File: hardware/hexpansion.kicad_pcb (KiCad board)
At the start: 2 copper layers, 86 x 45.6 mm, 87 parts, among them J1 Hexpansion-Connector, U1 AP3602AKTR-G1, U10 XL-0807RGBC-WS2812B-S, U11 XL-0807RGBC-WS2812B-S, U12 XL-0807RGBC-WS2812B-S, U13 XL-0807RGBC-WS2812B-S, U14 XL-0807RGBC-WS2812B-S, U15 XL-0807RGBC-WS2812B-S, U16 XL-0807RGBC-WS2812B-S, U17 XL-0807RGBC-WS2812B-S, U18 XL-0807RGBC-WS2812B-S, U19 XL-0807RGBC-WS2812B-S, U2 ZD24C64A-XGMT, U20 XL-0807RGBC-WS2812B-S, U21 XL-0807RGBC-WS2812B-S, U22 XL-0807RGBC-WS2812B-S, U23 XL-0807RGBC-WS2812B-S, U24 XL-0807RGBC-WS2812B-S, U25 XL-0807RGBC-WS2812B-S, U26 XL-0807RGBC-WS2812B-S, U27 XL-0807RGBC-WS2812B-S, U28 XL-0807RGBC-WS2812B-S, U29 XL-0807RGBC-WS2812B-S, U3 XL-0807RGBC-WS2812B-S, U30 XL-0807RGBC-WS2812B-S, U31 XL-0807RGBC-WS2812B-S, U32 XL-0807RGBC-WS2812B-S, U33 XL-0807RGBC-WS2812B-S, U34 XL-0807RGBC-WS2812B-S, U35 XL-0807RGBC-WS2812B-S, U36 XL-0807RGBC-WS2812B-S, U37 XL-0807RGBC-WS2812B-S, U38 XL-0807RGBC-WS2812B-S, U39 XL-0807RGBC-WS2812B-S, U4 XL-0807RGBC-WS2812B-S, U40 XL-0807RGBC-WS2812B-S, U41 XL-0807RGBC-WS2812B-S, U42 XL-0807RGBC-WS2812B-S, U43 XL-0807RGBC-WS2812B-S, U44 XL-0807RGBC-WS2812B-S, U45 XL-0807RGBC-WS2812B-S, U46 XL-0807RGBC-WS2812B-S, U47 XL-0807RGBC-WS2812B-S, U48 XL-0807RGBC-WS2812B-S, U49 XL-0807RGBC-WS2812B-S, U5 XL-0807RGBC-WS2812B-S, U50 XL-0807RGBC-WS2812B-S, U51 XL-0807RGBC-WS2812B-S, U52 XL-0807RGBC-WS2812B-S, U53 XL-0807RGBC-WS2812B-S, U54 XL-0807RGBC-WS2812B-S, U55 XL-0807RGBC-WS2812B-S, U56 XL-0807RGBC-WS2812B-S, U57 XL-0807RGBC-WS2812B-S, U58 XL-0807RGBC-WS2812B-S, U59 XL-0807RGBC-WS2812B-S, U6 XL-0807RGBC-WS2812B-S, U60 XL-0807RGBC-WS2812B-S, U61 XL-0807RGBC-WS2812B-S, U62 XL-0807RGBC-WS2812B-S, U63 XL-0807RGBC-WS2812B-S, U64 XL-0807RGBC-WS2812B-S, U65 XL-0807RGBC-WS2812B-S, U66 XL-0807RGBC-WS2812B-S, U67 XL-0807RGBC-WS2812B-S, U68 XL-0807RGBC-WS2812B-S, U69 XL-0807RGBC-WS2812B-S, U7 XL-0807RGBC-WS2812B-S, U70 XL-0807RGBC-WS2812B-S, U71 XL-0807RGBC-WS2812B-S, U72 XL-0807RGBC-WS2812B-S, U73 XL-0807RGBC-WS2812B-S, U74 XL-0807RGBC-WS2812B-S, U75 XL-0807RGBC-WS2812B-S, U76 XL-0807RGBC-WS2812B-S, U77 XL-0807RGBC-WS2812B-S, U78 XL-0807RGBC-WS2812B-S, U8 XL-0807RGBC-WS2812B-S, U9 XL-0807RGBC-WS2812B-S

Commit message: Fully routed
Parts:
- removed C3: 1uF, Capacitor_SMD:C_0603_1608Metric
- added D1: SS38BF, easyeda2kicad:SMBF_L4.3-W3.6-LS5.3-RD, F.Cu at (117.5, 107.8)
- added J2: Conn_01x03_Pin, Connector_Wire:SolderWire-0.1sqmm_1x03_P3.6mm_D0.4mm_OD1mm, B.Cu at (132.8, 78.5)
- added JP1: SolderJumper_2_Bridged, Jumper:SolderJumper-2_P1.3mm_Bridged_RoundedPad1.0x1.5mm, B.Cu at (162.6, 104.5)
- added L1: AFE201610S4R7MBT, easyeda2kicad:IND-SMD_L2.0-W1.6, F.Cu at (117.7, 101.6)
- added R4: 100k, Resistor_SMD:R_0603_1608Metric, F.Cu at (126.1, 108.6)
- added SW1: SKTAACE010, easyeda2kicad:KEY-SMD_4P-L2.6-W1.6-P0.80-LS3.0, F.Cu at (126.7, 78.4)
- added SW2: SKTAACE010, easyeda2kicad:KEY-SMD_4P-L2.6-W1.6-P0.80-LS3.0, F.Cu at (127.0, 120.4)
- added TP1: TestPoint, TestPoint:TestPoint_Pad_2.0x2.0mm, B.Cu at (126.5, 98.9)
- added TP2: TestPoint, TestPoint:TestPoint_Pad_2.0x2.0mm, B.Cu at (126.5, 113.9)
- added TP3: TestPoint, TestPoint:TestPoint_Pad_2.0x2.0mm, B.Cu at (175.4, 111.3)
- added TP4: TestPoint, TestPoint:TestPoint_Pad_2.0x2.0mm, B.Cu at (126.5, 85.5)
- C1, C2: value 1uF -> 22uF
- R1: value R -> 750k
- U1: value AP3602AKTR-G1 -> MT3608; footprint easyeda2kicad:SOT-23-6_L2.9-W1.6-P0.95-LS2.8-BR -> Package_TO_SOT_SMD:SOT-23-6
- moved C2 16.8 mm to (121.9, 108.6), turned to 180 degrees
- moved U4 14.3 mm to (135.1, 100.7), turned to 0 degrees
- moved U68 13.5 mm to (165.0, 113.1), turned to 0 degrees
- moved R1 12.4 mm to (129.3, 109.8), turned to -90 degrees
- moved U3 12.2 mm to (124.6, 90.9)
- moved U1 10.5 mm to (123.2, 103.7), turned to 90 degrees
- moved U67 9.97 mm to (164.9, 115.7), turned to 0 degrees
- moved U20 9.53 mm to (154.4, 100.3), turned to 0 degrees
- moved U78 9.26 mm to (141.2, 94.1), turned to 0 degrees
- moved U11 8.56 mm to (144.6, 102.6), turned to 0 degrees
- moved U69 8.04 mm to (165.0, 110.1), turned to 0 degrees
- moved U13 7.91 mm to (144.1, 95.9), turned to 0 degrees
- moved U12 7.90 mm to (144.4, 99.2), turned to 0 degrees
- moved U61 7.72 mm to (158.4, 107.8), turned to 0 degrees
- moved U63 7.68 mm to (161.9, 116.8), turned to 0 degrees
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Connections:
- C1 pad 1: Net-(U1-C+) -> /3V3
- C1 pad 2: Net-(U1-C-) -> /GND
- C2 pad 1: /3V3 -> /GND
- C2 pad 2: /GND -> +5V
- R1 pad 1: Net-(JP1-B) -> Net-(U1-FB)
- R1 pad 2: Net-(C4-Pad1) -> +5V
- U1 pad 1: +5C -> Net-(D1-A)
- U1 pad 3: /HS_H -> Net-(U1-FB)
- U1 pad 4: Net-(U1-C-) -> /3V3
- U1 pad 6: Net-(U1-C+) -> unconnected-(U1-NC-Pad6)
- U11 pad 3: Net-(U10-DO) -> Net-(U11-DI)
- U56 pad 3: unconnected-(U56-DI-Pad3) -> Net-(JP1-B)
- U60 pad 1: unconnected-(U60-DO-Pad1) -> Net-(U60-DO)
- U61 pad 3: unconnected-(U61-DI-Pad3) -> Net-(U60-DO)
- U65 pad 1: unconnected-(U65-DO-Pad1) -> Net-(U65-DO)
- U66 pad 3: unconnected-(U66-DI-Pad3) -> Net-(U65-DO)
- U70 pad 1: unconnected-(U70-DO-Pad1) -> Net-(U70-DO)
- U71 pad 3: unconnected-(U71-DI-Pad3) -> Net-(U70-DO)
- U75 pad 1: unconnected-(U75-DO-Pad1) -> Net-(U75-DO)
- U76 pad 2: unconnected-(U76-GND-Pad2) -> /GND
- U76 pad 3: unconnected-(U76-DI-Pad3) -> Net-(U75-DO)
- U77 pad 1: unconnected-(U77-DO-Pad1) -> Net-(U77-DO)
- U77 pad 2: unconnected-(U77-GND-Pad2) -> /GND
- U78 pad 1: unconnected-(U78-DO-Pad1) -> Net-(U11-DI)
- U78 pad 2: unconnected-(U78-GND-Pad2) -> /GND
- U78 pad 3: unconnected-(U78-DI-Pad3) -> Net-(U10-DO)
- U78 pad 4: unconnected-(U78-VDD-Pad4) -> +5V
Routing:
- net +5V: track 47.2 -> 541.1 mm, vias 0 -> 4
- net /GND: track 85.0 -> 538.5 mm, vias 8 -> 19
- net Net-(J1-HS_G): track 0.00 -> 52.4 mm, vias 0 -> 2
- net /HS_H: track 37.8 -> 0.00 mm
- net /HS_I: track 28.9 -> 61.1 mm
- net Net-(U53-DO): track 0.00 -> 31.7 mm, vias 0 -> 2
- net Net-(U39-DO): track 0.00 -> 30.8 mm, vias 0 -> 2
- net /3V3: track 43.9 -> 74.3 mm, vias 0 -> 1
- net Net-(U46-DO): track 0.00 -> 26.6 mm, vias 0 -> 2
- net Net-(U32-DO): track 0.00 -> 25.9 mm, vias 0 -> 2
- net Net-(U26-DO): track 0.00 -> 21.7 mm, vias 0 -> 2
- net Net-(U62-DO): track 0.00 -> 19.5 mm, vias 0 -> 2
- net Net-(U70-DO): track 0.00 -> 18.6 mm, vias 0 -> 2
- net Net-(U57-DO): track 0.00 -> 17.9 mm, vias 0 -> 2
- net Net-(U74-DO): track 0.00 -> 17.7 mm, vias 0 -> 2
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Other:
- board size 86 x 45.6 mm -> 86.8 x 46 mm
- board text removed: "${REFERENCE}"

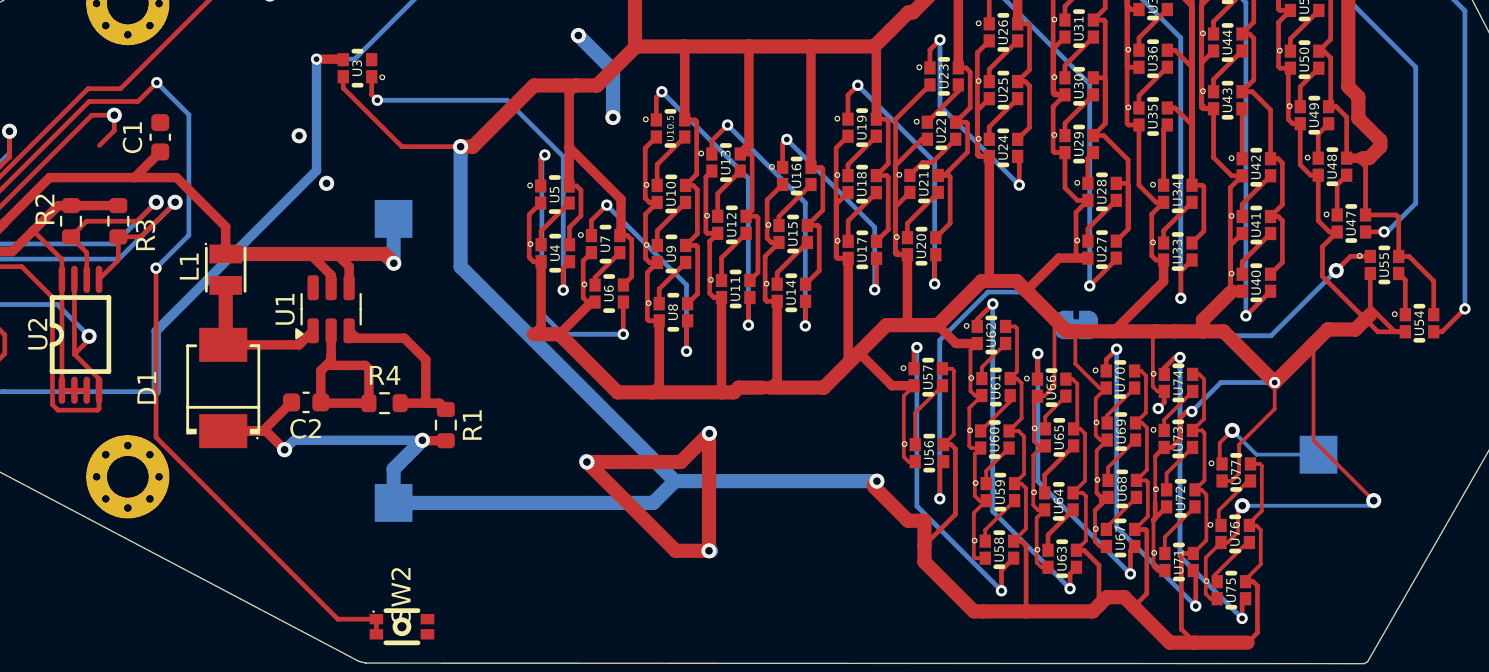
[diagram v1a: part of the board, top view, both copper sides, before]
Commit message: Improve decoupling of power supply
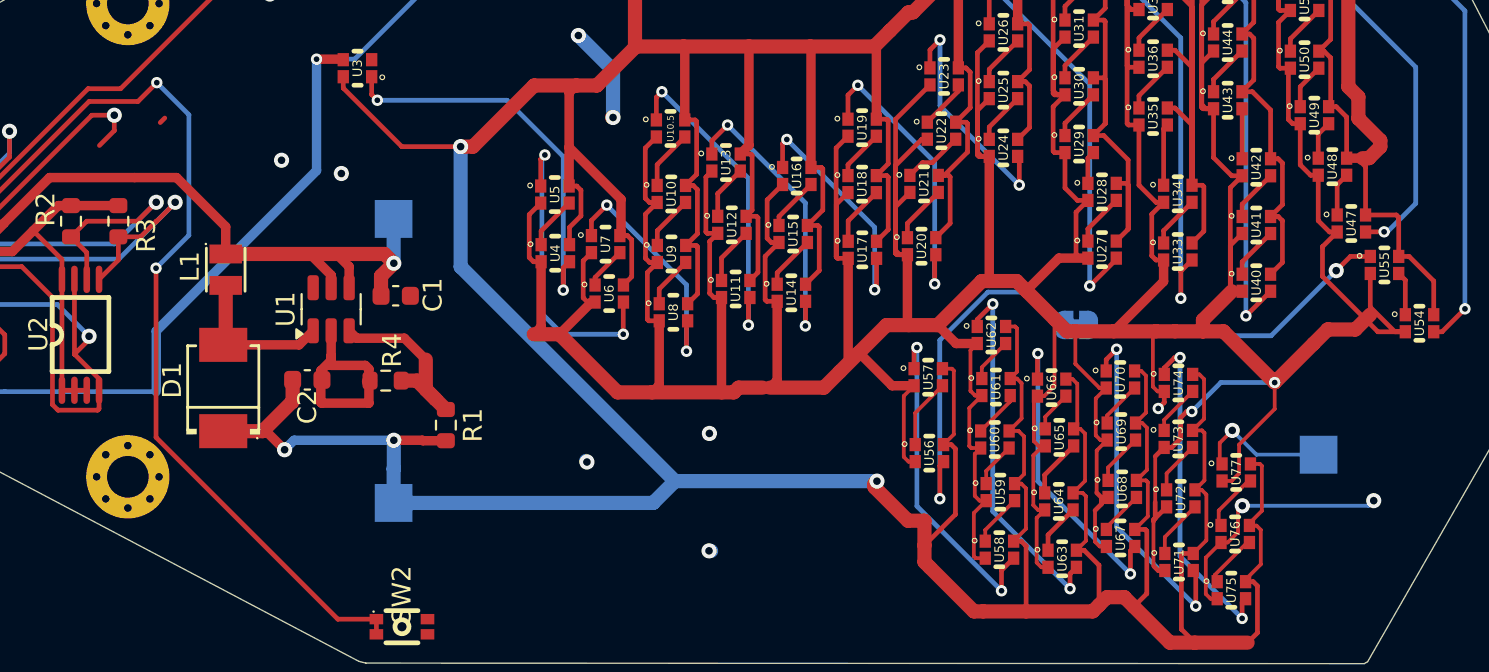
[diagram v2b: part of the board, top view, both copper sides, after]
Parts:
- moved C1 15.0 mm to (126.7, 102.9), turned to 0 degrees
- moved C2 1.19 mm to (122.0, 107.4)
- moved R4 1.19 mm to (126.1, 107.4)
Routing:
- net /GND: track 538.5 -> 507.3 mm
- net Net-(U1-FB): track 9.53 -> 10.4 mm
- net +5V: track 541.1 -> 541.6 mm

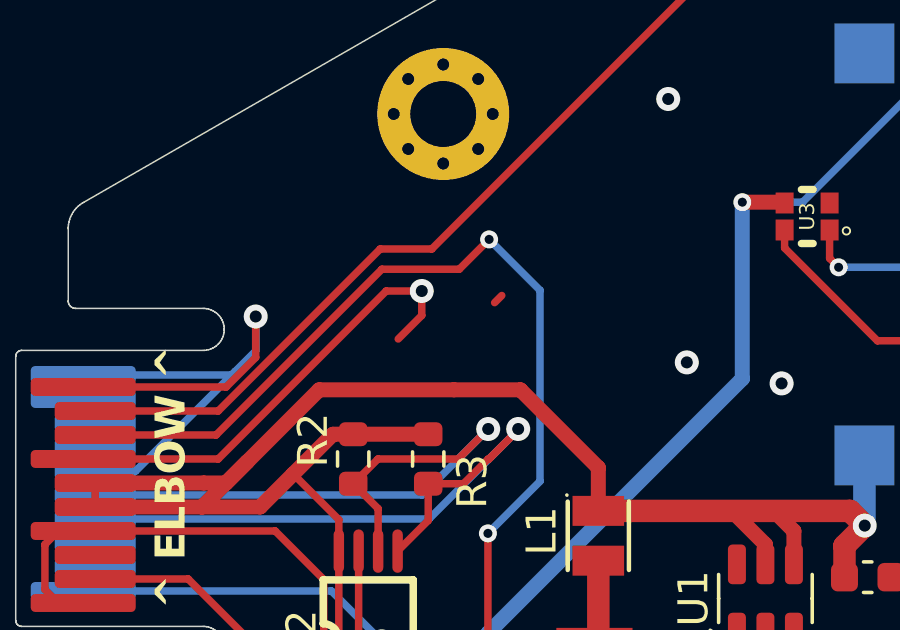
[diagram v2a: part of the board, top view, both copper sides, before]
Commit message: Remove extraneous trace
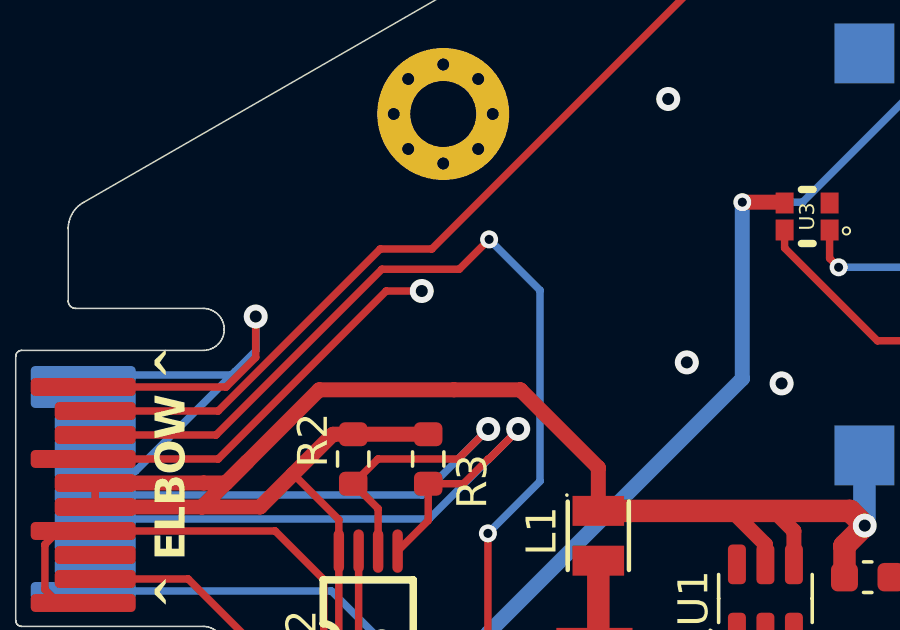
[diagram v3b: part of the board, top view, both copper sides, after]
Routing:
- net /GND: track 507.3 -> 505.0 mm
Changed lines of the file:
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@@
-	)
-	(segment
-		(start 114.452373 93.55)
-		(end 114.212876 93.789497)
-		(width 0.25)
-		(layer "F.Cu")
-		(net 1)
 	)
 	(segment
@@
 	)
 	(segment
-		(start 111.785214 94.214786)
-		(end 111 95)
-		(width 0.25)
-		(layer "F.Cu")
-		(net 1)
-	)
-	(segment
 		(start 163.629 108.361)
 		(end 164.18 107.81)
@@
 		(width 0.25)
 		(layer "F.Cu")
-		(net 1)
-	)
-	(segment
-		(start 111.785214 93.40067)
-		(end 111.785214 94.214786)
-		(width 0.25)
-		(layer "F.Cu")
